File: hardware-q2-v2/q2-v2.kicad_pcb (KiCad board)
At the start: 6 copper layers, 46 x 76 mm, 198 parts, among them CN1 PJ-342B-TX-SMT, CN2 Solder wire pads, CN3 Solder wire pads, Q101 BSS138, Q102 BSS138, Q103 BSS138, Q104 BSS138, Q105 BSS138, Q106 MMBT3904, Q107 MMBT3904, U1 RX8130CE:BB, U10 W25Q128JVSIQ, U11 DRV2605LDGSR, U12 CH343P, U14 STC3115AIQT, U15 LSM6DS3TR-C, U17 SGM7229YMS10G/TR, U2 CS43131-CNZ, U20 TLV75533PDBVR, U21 SN74LVC1G123DCUR, U3 DSCB_BQ25895RTW, U4 TLV62568DBVR, U5 ME6211C18M5G-N, U6 GEK100, U7 PCA9306DQER, U8 SN74LV4T125RGYR, U9 ESP32-S31NRV16, X1 26MHz, Y101 40MHz 15pF 10ppm MDH 2.3.3.40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

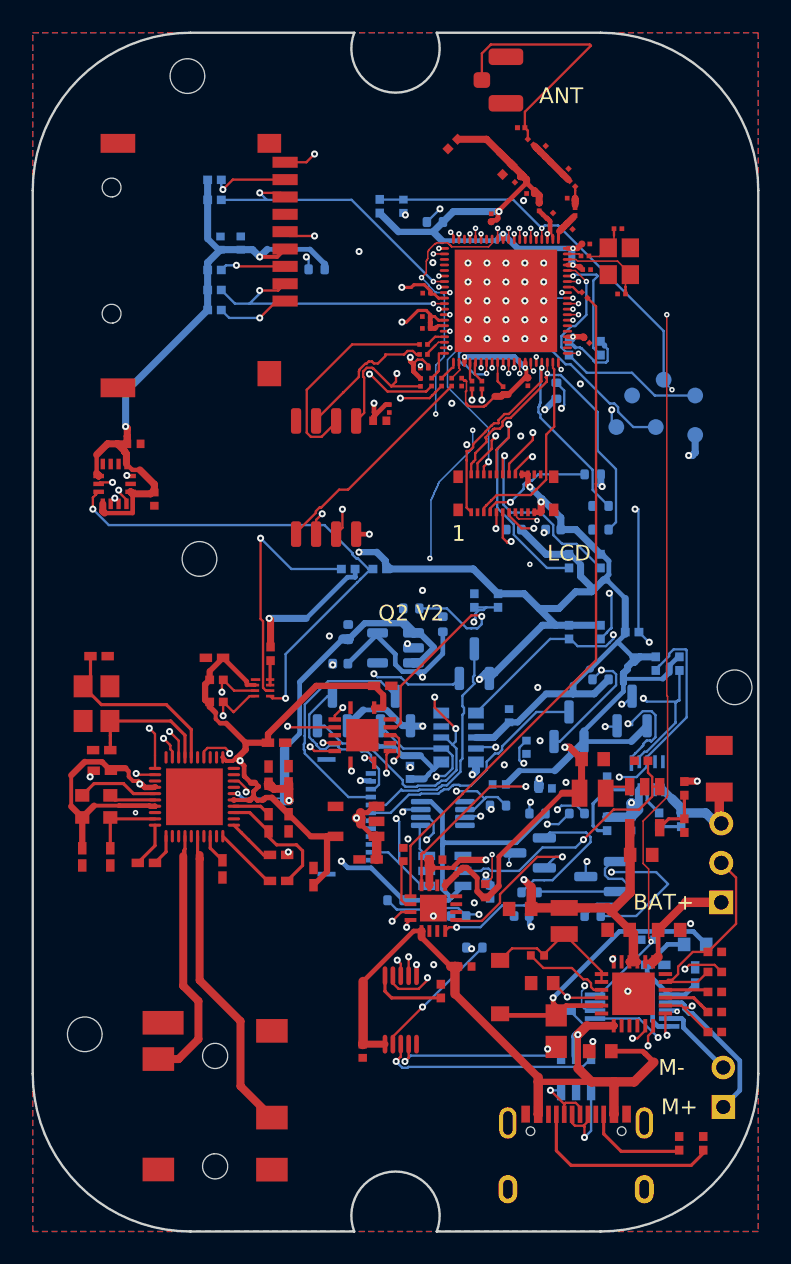
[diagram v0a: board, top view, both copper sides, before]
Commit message: feat: convert V2 passives to 0402 and retain power-only routing
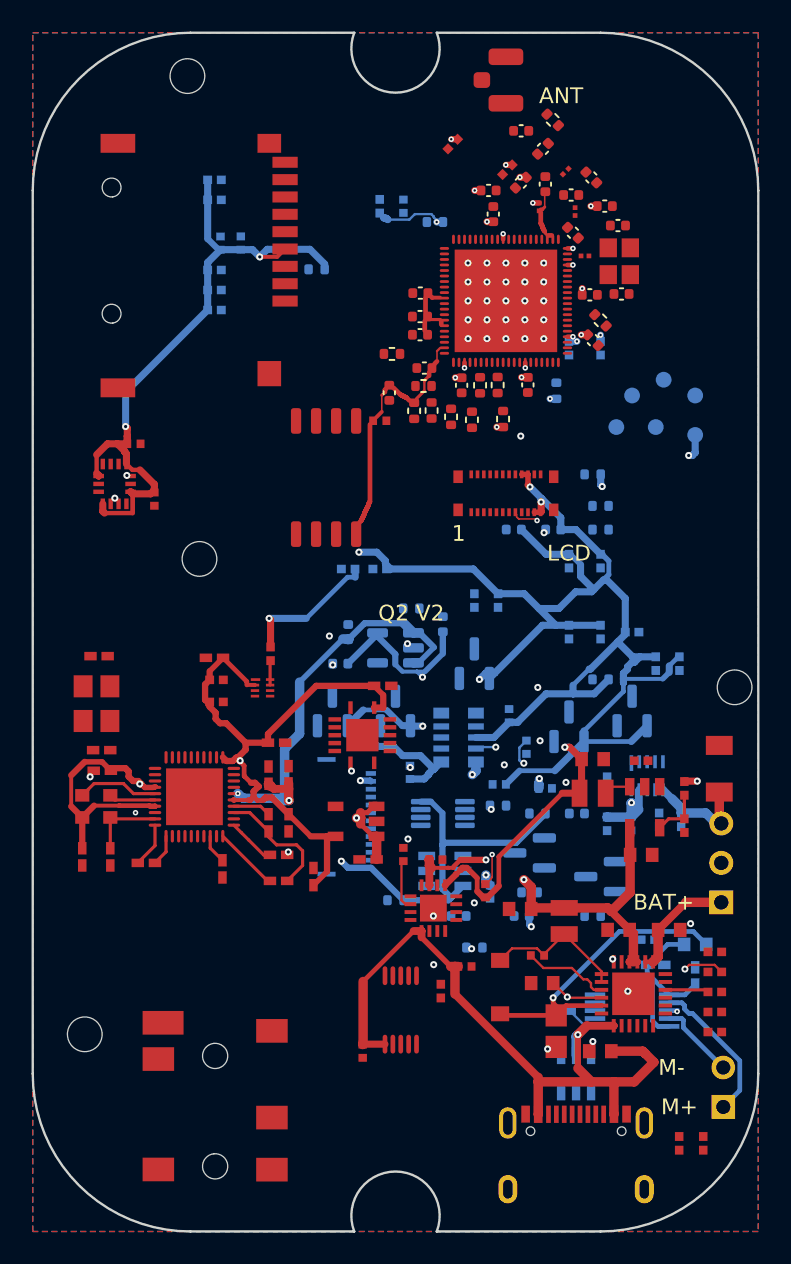
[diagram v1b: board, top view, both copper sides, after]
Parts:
- moved C106 2.68 mm to (165.1, 78.6)
- moved C117 2.67 mm to (157.8, 77.6), turned to 0 degrees
- moved R104 2.28 mm to (155.4, 92.0)
- moved R109 2.20 mm to (156.7, 92.2)
- moved R101 2.09 mm to (151.6, 88.0)
- moved C118 2.03 mm to (161.4, 77.2), turned to 90 degrees
- moved R102 2.00 mm to (153.6, 90.0)
- moved L105 1.98 mm to (161.8, 73.2)
- moved R106 1.89 mm to (164.9, 85.9)
- moved R107 1.84 mm to (153.1, 91.6)
- moved R105 1.81 mm to (157.2, 90.0)
- moved R103 1.80 mm to (154.2, 91.6)
- moved R110 1.80 mm to (158.7, 92.1)
- moved C105 1.61 mm to (164.2, 84.3)
- moved C107 1.26 mm to (164.3, 76.8)
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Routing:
- net SYS_I2C_SCL: track 103.6 -> 0.00 mm, vias 5 -> 0
- net SYS_I2C_SDA: track 101.3 -> 0.00 mm, vias 7 -> 0
- net CHG_OTG_EN: track 66.2 -> 0.00 mm, vias 2 -> 0
- net USB_PATH_SEL: track 66.1 -> 0.00 mm, vias 4 -> 0
- net AUDIO_I2C_SDA: track 65.0 -> 0.00 mm, vias 3 -> 0
- net CHG_INT_N: track 65.0 -> 0.00 mm, vias 4 -> 0
- net MOTOR_EN: track 63.4 -> 0.00 mm, vias 3 -> 0
- net CHIP_PU: track 62.7 -> 0.00 mm, vias 4 -> 0
- net VCC_3V3: track 301.6 -> 243.1 mm, vias 20 -> 34
- net BOOT_DOWNLOAD_N: track 54.7 -> 0.00 mm, vias 2 -> 0
- net AUDIO_I2C_SCL: track 51.6 -> 0.00 mm, vias 3 -> 0
- net CTRL_RESET_N: track 50.0 -> 0.00 mm, vias 2 -> 0
- net KEY_POWER_SENSE_N: track 48.2 -> 0.00 mm, vias 3 -> 0
- net IMU_INT1: track 46.9 -> 0.00 mm, vias 2 -> 0
- net BAT_ALERT_N: track 46.6 -> 0.00 mm, vias 3 -> 0
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
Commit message: fix: standardize V2 0402 resistor and capacitor footprints
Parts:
- C101: footprint V2:FP_C101 -> V2:C_0402_1005Metric
- C102: footprint V2:FP_C102 -> V2:C_0402_1005Metric
- C103: footprint V2:FP_C103 -> V2:C_0402_1005Metric
- C104: footprint V2:FP_C104 -> V2:C_0402_1005Metric
- C105: footprint V2:FP_C105 -> V2:C_0402_1005Metric
- C106: footprint V2:FP_C106 -> V2:C_0402_1005Metric
- C107: footprint V2:FP_C107 -> V2:C_0402_1005Metric
- C108: footprint V2:FP_C108 -> V2:C_0402_1005Metric
- C109: footprint V2:FP_C109 -> V2:C_0402_1005Metric
- C11: footprint V2:FP_C11 -> V2:C_0402_1005Metric
- C110: footprint V2:FP_C110 -> V2:C_0402_1005Metric
- C113: footprint V2:FP_C113 -> V2:C_0402_1005Metric
- C114: footprint V2:FP_C114 -> V2:C_0402_1005Metric
- C115: footprint V2:FP_C115 -> V2:C_0402_1005Metric
- C116: footprint V2:FP_C116 -> V2:C_0402_1005Metric
- C117: footprint V2:FP_C117 -> V2:C_0402_1005Metric
- C118: footprint V2:FP_C118 -> V2:C_0402_1005Metric
- C119: footprint V2:FP_C119 -> V2:C_0402_1005Metric
- C120: footprint V2:FP_C120 -> V2:C_0402_1005Metric
- C121: footprint V2:FP_C121 -> V2:C_0402_1005Metric
- C122: footprint V2:FP_C122 -> V2:C_0402_1005Metric
- C123: footprint V2:FP_C123 -> V2:C_0402_1005Metric
- C124: footprint V2:FP_C124 -> V2:C_0402_1005Metric
- C125: footprint V2:FP_C125 -> V2:C_0402_1005Metric
- C13: footprint V2:FP_C13 -> V2:C_0402_1005Metric
- C130: footprint V2:FP_C130 -> V2:C_0402_1005Metric
- C131: footprint V2:FP_C131 -> V2:C_0402_1005Metric
- C132: footprint V2:FP_C132 -> V2:C_0402_1005Metric
- C133: footprint V2:FP_C133 -> V2:C_0402_1005Metric
- C134: footprint V2:FP_C134 -> V2:C_0402_1005Metric
- C135: footprint V2:FP_C135 -> V2:C_0402_1005Metric
- C136: footprint V2:FP_C136 -> V2:C_0402_1005Metric
- C137: footprint V2:FP_C137 -> V2:C_0402_1005Metric
- C17: footprint V2:FP_C17 -> V2:C_0402_1005Metric
- C19: footprint V2:FP_C19 -> V2:C_0402_1005Metric
- C20: footprint V2:FP_C20 -> V2:C_0402_1005Metric
- C21: footprint V2:FP_C21 -> V2:C_0402_1005Metric
- C22: footprint V2:FP_C22 -> V2:C_0402_1005Metric
- C23: footprint V2:FP_C23 -> V2:C_0402_1005Metric
- C24: footprint V2:FP_C24 -> V2:C_0402_1005Metric
- C25: footprint V2:FP_C25 -> V2:C_0402_1005Metric
- C26: footprint V2:FP_C26 -> V2:C_0402_1005Metric
- C27: footprint V2:FP_C27 -> V2:C_0402_1005Metric
- C28: footprint V2:FP_C28 -> V2:C_0402_1005Metric
- C29: footprint V2:FP_C29 -> V2:C_0402_1005Metric
- C3: footprint V2:FP_C3 -> V2:C_0402_1005Metric
- C30: footprint V2:FP_C30 -> V2:C_0402_1005Metric
- C31: footprint V2:FP_C31 -> V2:C_0402_1005Metric
- C32: footprint V2:FP_C32 -> V2:C_0402_1005Metric
- C33: footprint V2:FP_C33 -> V2:C_0402_1005Metric
- C34: footprint V2:FP_C34 -> V2:C_0402_1005Metric
- C35: footprint V2:FP_C35 -> V2:C_0402_1005Metric
- C36: footprint V2:FP_C36 -> V2:C_0402_1005Metric
- C37: footprint V2:FP_C37 -> V2:C_0402_1005Metric
- C38: footprint V2:FP_C38 -> V2:C_0402_1005Metric
- C39: footprint V2:FP_C39 -> V2:C_0402_1005Metric
- C4: footprint V2:FP_C4 -> V2:C_0402_1005Metric
- C43: footprint V2:FP_C43 -> V2:C_0402_1005Metric
- C44: footprint V2:FP_C44 -> V2:C_0402_1005Metric
- C47: footprint V2:FP_C47 -> V2:C_0402_1005Metric
- C48: footprint V2:FP_C48 -> V2:C_0402_1005Metric
- C49: footprint V2:FP_C49 -> V2:C_0402_1005Metric
- C5: footprint V2:FP_C5 -> V2:C_0402_1005Metric
- C50: footprint V2:FP_C50 -> V2:C_0402_1005Metric
- C51: footprint V2:FP_C51 -> V2:C_0402_1005Metric
- C53: footprint V2:FP_C53 -> V2:C_0402_1005Metric
- C54: footprint V2:FP_C54 -> V2:C_0402_1005Metric
- C58: footprint V2:FP_C58 -> V2:C_0402_1005Metric
- C59: footprint V2:FP_C59 -> V2:C_0402_1005Metric
- C6: footprint V2:FP_C6 -> V2:C_0402_1005Metric
- C61: footprint V2:FP_C61 -> V2:C_0402_1005Metric
- C7: footprint V2:FP_C7 -> V2:C_0402_1005Metric
- L105: footprint V2:FP_L105 -> V2:R_0402_1005Metric
- R10: footprint V2:FP_R10 -> V2:R_0402_1005Metric
- R101: footprint V2:FP_R101 -> V2:R_0402_1005Metric
- R102: footprint V2:FP_R102 -> V2:R_0402_1005Metric
- R103: footprint V2:FP_R103 -> V2:R_0402_1005Metric
- R104: footprint V2:FP_R104 -> V2:R_0402_1005Metric
- R105: footprint V2:FP_R105 -> V2:R_0402_1005Metric
- R106: footprint V2:FP_R106 -> V2:R_0402_1005Metric
- R107: footprint V2:FP_R107 -> V2:R_0402_1005Metric
- R108: footprint V2:FP_R108 -> V2:R_0402_1005Metric
- R109: footprint V2:FP_R109 -> V2:R_0402_1005Metric
- R11: footprint V2:FP_R11 -> V2:R_0402_1005Metric
- R110: footprint V2:FP_R110 -> V2:R_0402_1005Metric
- R12: footprint V2:FP_R12 -> V2:R_0402_1005Metric
- R120: footprint V2:FP_R120 -> V2:R_0402_1005Metric
- R121: footprint V2:FP_R121 -> V2:R_0402_1005Metric
- R122: footprint V2:FP_R122 -> V2:R_0402_1005Metric
- R123: footprint V2:FP_R123 -> V2:R_0402_1005Metric
- R124: footprint V2:FP_R124 -> V2:R_0402_1005Metric
- R125: footprint V2:FP_R125 -> V2:R_0402_1005Metric
- R126: footprint V2:FP_R126 -> V2:R_0402_1005Metric
- R127: footprint V2:FP_R127 -> V2:R_0402_1005Metric
- R128: footprint V2:FP_R128 -> V2:R_0402_1005Metric
- R129: footprint V2:FP_R129 -> V2:R_0402_1005Metric
- R13: footprint V2:FP_R13 -> V2:R_0402_1005Metric
- R130: footprint V2:FP_R130 -> V2:R_0402_1005Metric
- R131: footprint V2:FP_R131 -> V2:R_0402_1005Metric
- R132: footprint V2:FP_R132 -> V2:R_0402_1005Metric
- R133: footprint V2:FP_R133 -> V2:R_0402_1005Metric
- R14: footprint V2:FP_R14 -> V2:R_0402_1005Metric
- R17: footprint V2:FP_R17 -> V2:R_0402_1005Metric
- R18: footprint V2:FP_R18 -> V2:R_0402_1005Metric
- R19: footprint V2:FP_R19 -> V2:R_0402_1005Metric
- R2: footprint V2:FP_R2 -> V2:R_0402_1005Metric
- R20: footprint V2:FP_R20 -> V2:R_0402_1005Metric
- R21: footprint V2:FP_R21 -> V2:R_0402_1005Metric
- R22: footprint V2:FP_R22 -> V2:R_0402_1005Metric
- R25: footprint V2:FP_R25 -> V2:R_0402_1005Metric
- R26: footprint V2:FP_R26 -> V2:R_0402_1005Metric
- R29: footprint V2:FP_R29 -> V2:R_0402_1005Metric
- R3: footprint V2:FP_R3 -> V2:R_0402_1005Metric
- R30: footprint V2:FP_R30 -> V2:R_0402_1005Metric
- R31: footprint V2:FP_R31 -> V2:R_0402_1005Metric
- R32: footprint V2:FP_R32 -> V2:R_0402_1005Metric
- R33: footprint V2:FP_R33 -> V2:R_0402_1005Metric
- R34: footprint V2:FP_R34 -> V2:R_0402_1005Metric
- R35: footprint V2:FP_R35 -> V2:R_0402_1005Metric
- R36: footprint V2:FP_R36 -> V2:R_0402_1005Metric
- R37: footprint V2:FP_R37 -> V2:R_0402_1005Metric
- R38: footprint V2:FP_R38 -> V2:R_0402_1005Metric
- R39: footprint V2:FP_R39 -> V2:R_0402_1005Metric
- R4: footprint V2:FP_R4 -> V2:R_0402_1005Metric
- R42: footprint V2:FP_R42 -> V2:R_0402_1005Metric
- R43: footprint V2:FP_R43 -> V2:R_0402_1005Metric
- R44: footprint V2:FP_R44 -> V2:R_0402_1005Metric
- R45: footprint V2:FP_R45 -> V2:R_0402_1005Metric
- R46: footprint V2:FP_R46 -> V2:R_0402_1005Metric
- R5: footprint V2:FP_R5 -> V2:R_0402_1005Metric
- R6: footprint V2:FP_R6 -> V2:R_0402_1005Metric
- R7: footprint V2:FP_R7 -> V2:R_0402_1005Metric
- R8: footprint V2:FP_R8 -> V2:R_0402_1005Metric
- R9: footprint V2:FP_R9 -> V2:R_0402_1005Metric
- moved C37 0.20 mm to (157.6, 122.2)
- moved C54 0.16 mm to (160.2, 112.8)
- moved C115 0.15 mm to (159.1, 76.3)
- moved C39 0.10 mm to (152.4, 78.5)
- moved R44 0.10 mm to (167.9, 125.2)
- moved R13 0.10 mm to (172.1, 127.3)

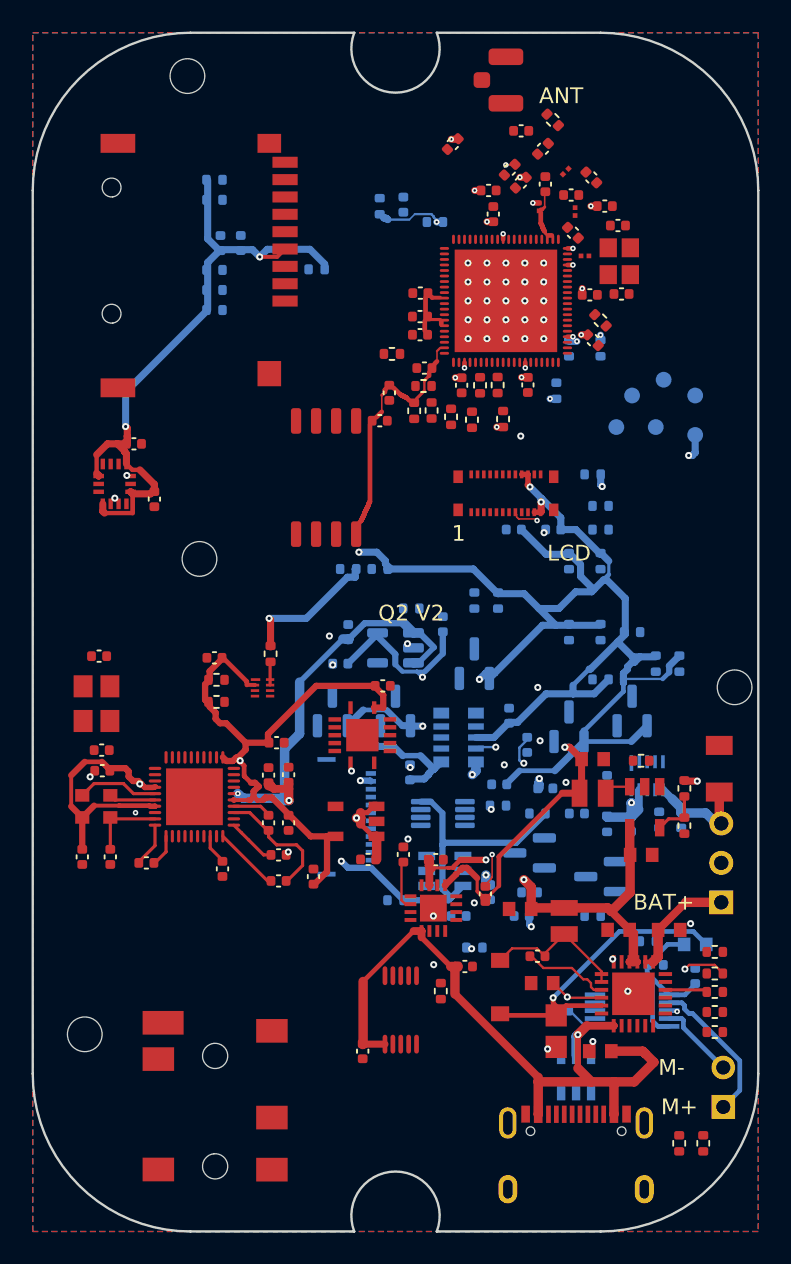
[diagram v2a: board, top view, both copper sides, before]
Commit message: feat: distribute V2 power through copper pours and local vias
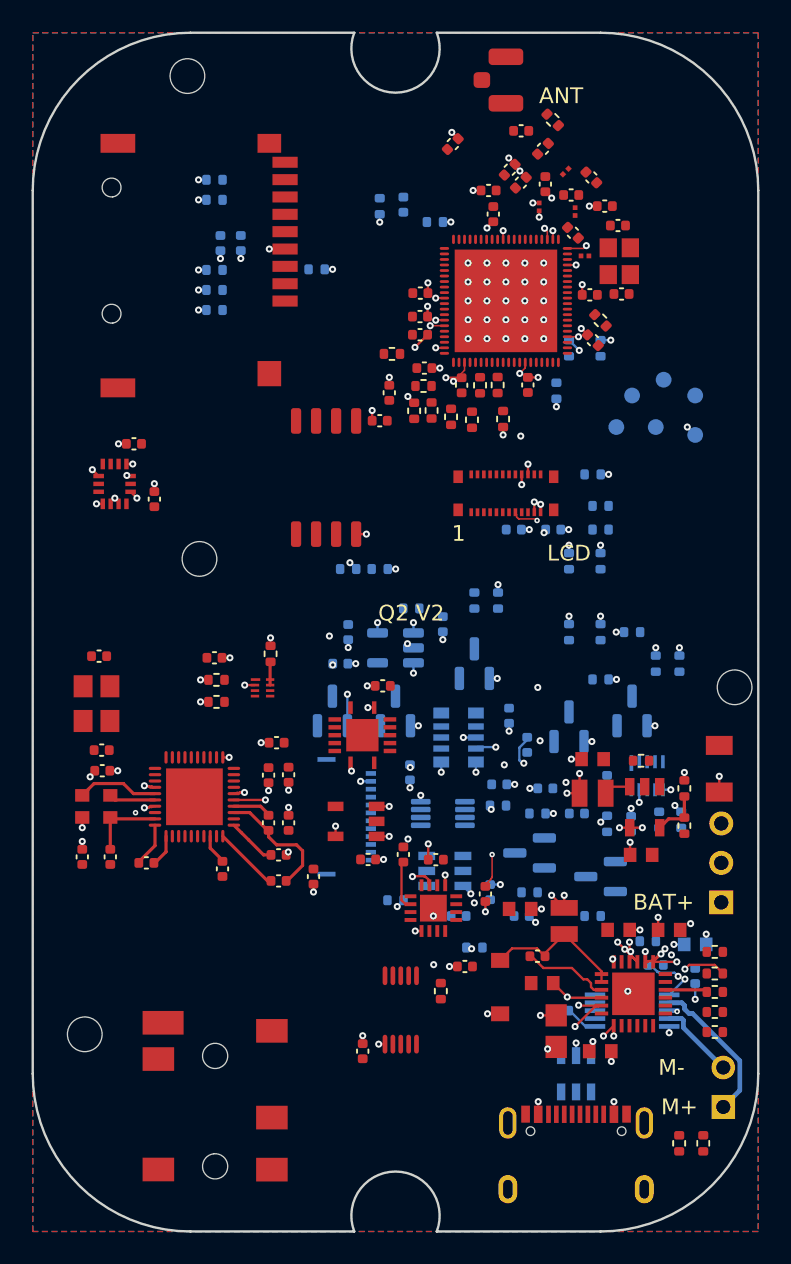
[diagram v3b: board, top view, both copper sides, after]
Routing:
- net VCC_3V3: track 243.1 -> 45.6 mm, vias 34 -> 74
- net VCC_3V3_AON: track 63.8 -> 5.04 mm, vias 4 -> 9
- net VBUS_5V: track 64.7 -> 8.92 mm, vias 2 -> 12
- net VCC_1V8: track 63.1 -> 10.7 mm, vias 2 -> 17
- net VCC: track 66.5 -> 16.6 mm, vias 5 -> 21
- net VBAT: track 33.8 -> 8.26 mm, vias 3 -> 10
- net VCC_PMID: track 19.6 -> 6.13 mm, vias 1 -> 5
- net MCU_VDD_SPI: track 13.0 -> 3.42 mm, vias 0 -> 6
- net N_5N15: track 11.2 -> 5.66 mm, vias 0 -> 5
- net GBAT: track 6.81 -> 2.07 mm, vias 0 -> 3
- net MCU_1V8: track 2.87 -> 4.43 mm, vias 0 -> 6
- net MCU_VDDA34: track 2.93 -> 2.29 mm, vias 0 -> 4
- net GND: vias 55 -> 56
- added copper zone on In3.Cu, net GBAT
- added copper zone on In3.Cu, net MCU_1V8
- added copper zone on In3.Cu, net MCU_VDDA34
- added copper zone on In3.Cu, net MCU_VDD_SPI
- added copper zone on In2.Cu, net N_5N15
- added copper zone on In3.Cu, net N_5N15
- added copper zone on In3.Cu, net VBAT
- added copper zone on In2.Cu, net VBUS_5V
- added copper zone on In3.Cu, net VBUS_5V
- added copper zone on In2.Cu, net VCC
- added copper zone on In3.Cu, net VCC
- added copper zone on In3.Cu, net VCC_1V8
- added copper zone on In3.Cu, net VCC_3V3
- added copper zone on In2.Cu, net VCC_3V3_AON
- added copper zone on In3.Cu, net VCC_3V3_AON
- added copper zone on In3.Cu, net VCC_PMID
